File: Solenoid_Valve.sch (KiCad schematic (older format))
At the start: 60 parts, among them IC1 Si8621AB-B-ISR, J1 Conn_01x02, J10 Conn_01x05, J11 Conn_01x02, J12 Conn_01x02, J13 Conn_01x02, J14 Conn_01x02, J15 Conn_01x02, J16 Conn_01x02, J17 Conn_01x02, J18 Conn_01x02, J19 Conn_01x02, J2 Conn_01x02, J20 Bus_mechaken_PCIexpress_x16_1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, J3 Conn_01x02, J4 Conn_01x02, J5 Conn_01x03, J6 Conn_01x02, J7 Conn_01x02, J8 Conn_01x02, J9 Conn_01x02, Q1 ULN2004D1013TR, Q2 ULN2004D1013TR, Q3 ULN2004D1013TR, U1 NJM7812, U2 AP2210N-3.3TRG1, U3 STM32F042K6Tx, U4 AP2210N-3.3TRG1, U5 MCP2562-E-SN

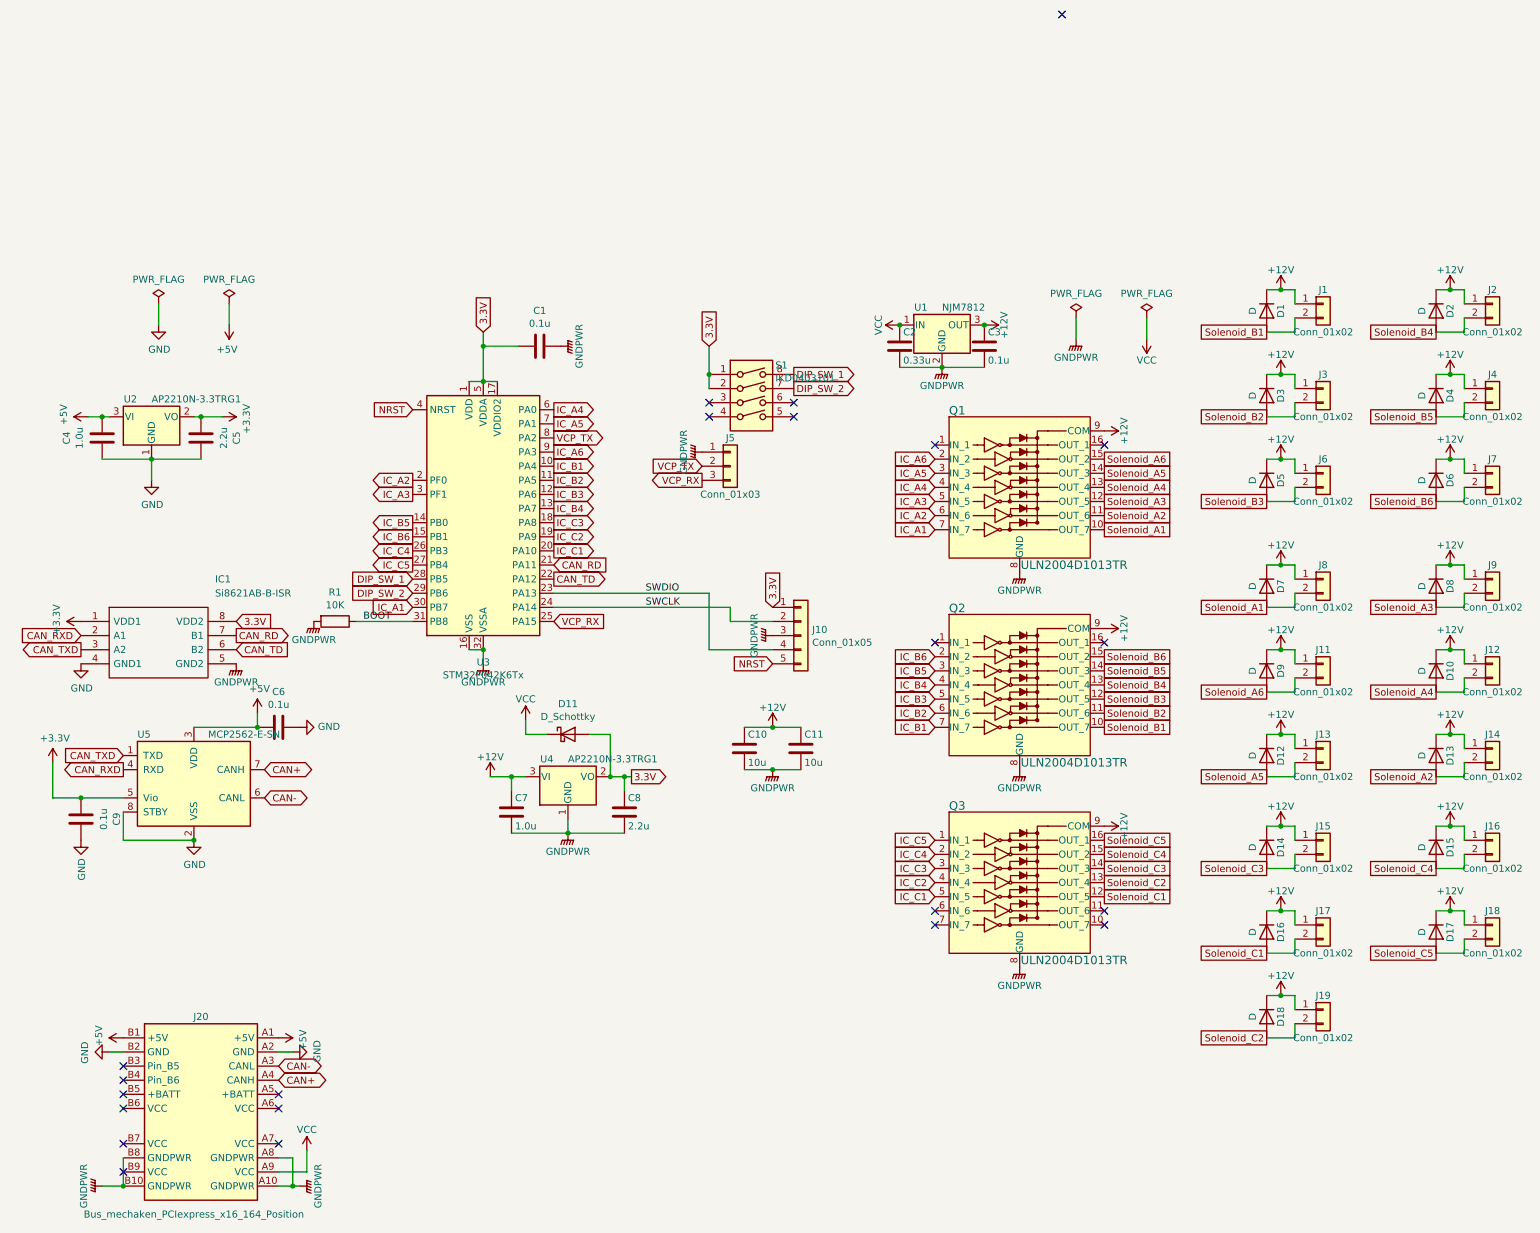
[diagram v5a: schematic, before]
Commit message: Fix: Symbol & Footprint Library
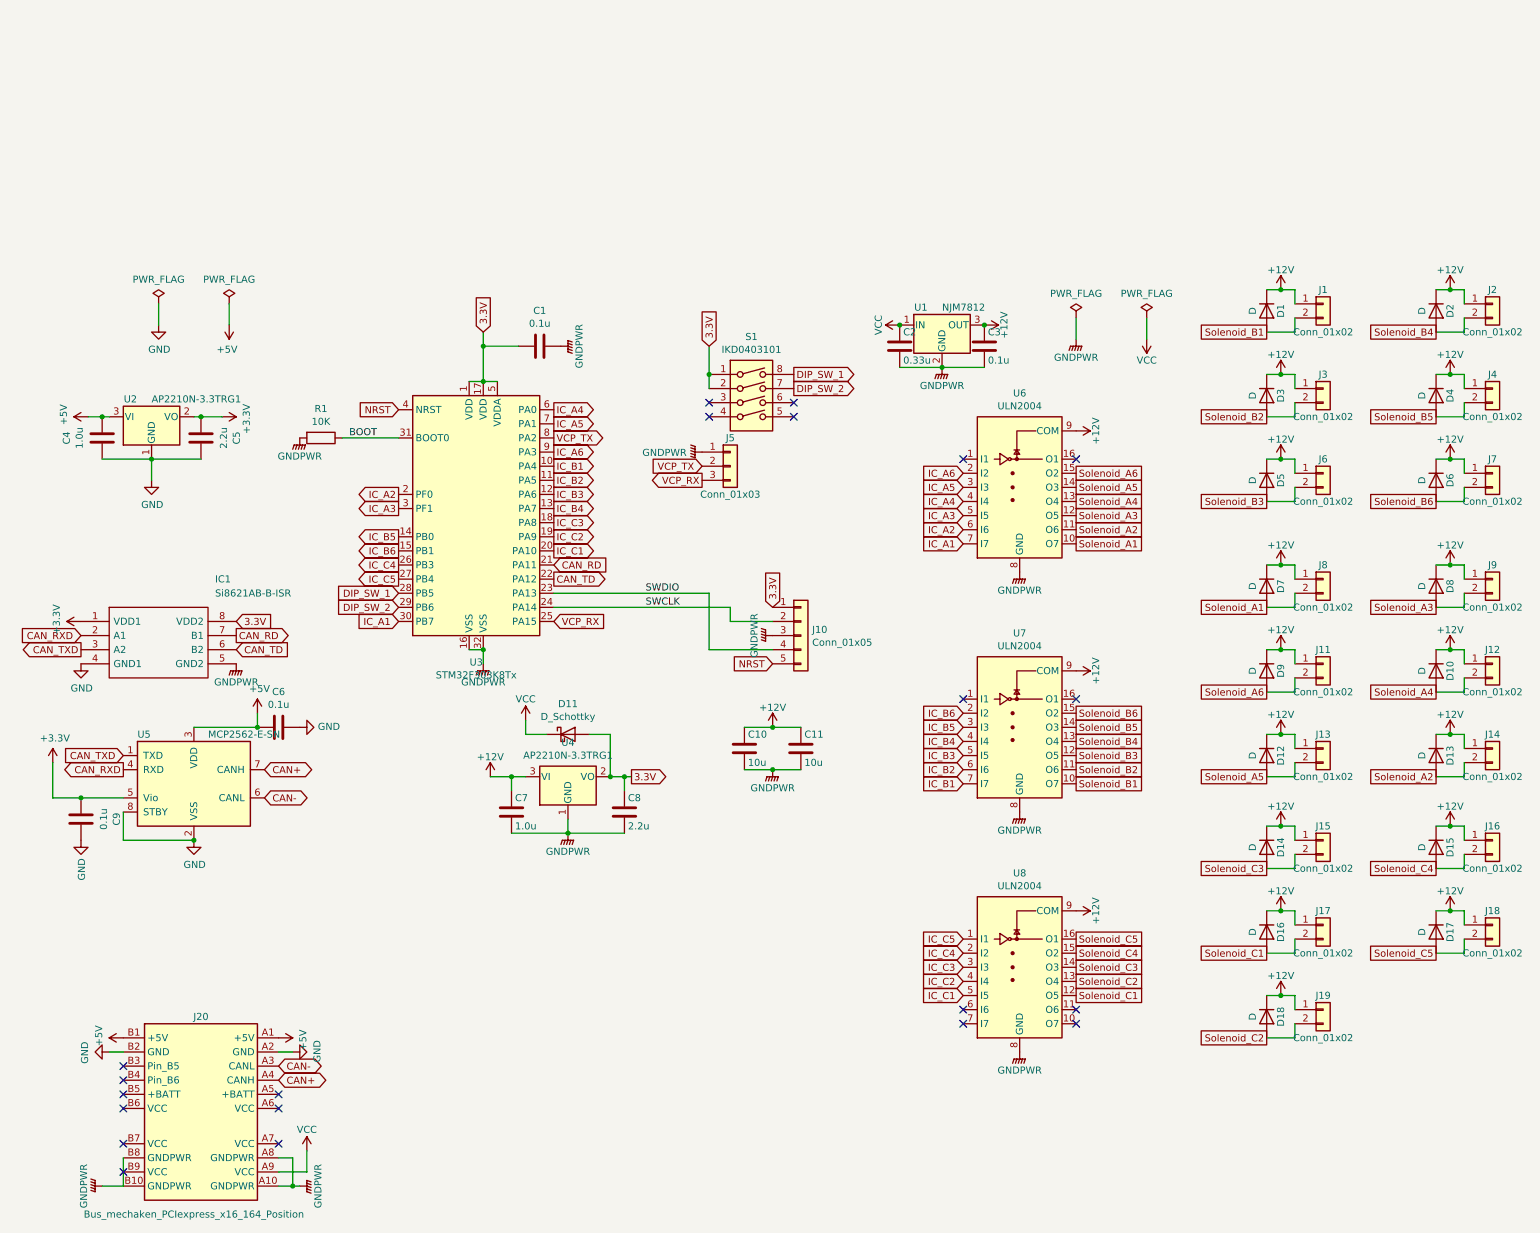
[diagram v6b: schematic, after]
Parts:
- removed Q1, Q2, Q3: ULN2004D1013TR, digikey-footprints:SOIC-16_W3.90mm, symbol Solenoid_Valve-rescue:ULN2003D1013TR-dk_Transistors-Bipolar-BJT-Arrays
- removed U3: STM32F042K6Tx, Package_QFP:LQFP-32_7x7mm_P0.8mm, symbol MCU_ST_STM32F0:STM32F042K6Tx
- added U3: STM32F303K8Tx, Package_QFP:LQFP-32_7x7mm_P0.8mm, symbol MCU_ST_STM32F3:STM32F303K8Tx
- added U6, U7, U8: ULN2004, Package_SO:SOIC-16_3.9x9.9mm_P1.27mm, symbol Transistor_Array:ULN2004
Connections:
- net +12V: now also U6.9 (COM), U7.9 (COM), U8.9 (COM)
- net 3.3V: now also U3.1 (VDD), U3.17 (VDD), U3.5 (VDDA)
- net BOOT: now also U3.31 (BOOT0)
- net CAN_RD: now also U3.21 (PA11)
- net CAN_TD: now also U3.22 (PA12)
- net DIP_SW_1: now also U3.28 (PB5)
- net DIP_SW_2: now also U3.29 (PB6)
- net GNDPWR: now also U3.16 (VSS), U3.32 (VSS), U6.8 (GND), U7.8 (GND), U8.8 (GND)
- net IC_A1: now also U3.30 (PB7), U6.7 (I7)
- net IC_A2: now also U3.2 (PF0), U6.6 (I6)
- net IC_A3: now also U3.3 (PF1), U6.5 (I5)
- net IC_A4: now also U3.6 (PA0), U6.4 (I4)
- net IC_A5: now also U3.7 (PA1), U6.3 (I3)
- net IC_A6: now also U3.9 (PA3), U6.2 (I2)
- net IC_B1: now also U3.10 (PA4), U7.7 (I7)
- net IC_B2: now also U3.11 (PA5), U7.6 (I6)
- net IC_B3: now also U3.12 (PA6), U7.5 (I5)
- net IC_B4: now also U3.13 (PA7), U7.4 (I4)
- net IC_B5: now also U3.14 (PB0), U7.3 (I3)
- net IC_B6: now also U3.15 (PB1), U7.2 (I2)
- net IC_C1: now also U3.20 (PA10), U8.5 (I5)
- net IC_C2: now also U3.19 (PA9), U8.4 (I4)
- net IC_C3: now also U3.18 (PA8), U8.3 (I3)
- net IC_C4: now also U3.26 (PB3), U8.2 (I2)
- net IC_C5: now also U3.27 (PB4), U8.1 (I1)
- net NRST: now also U3.4 (NRST)
- net SWCLK: now also U3.24 (PA14)
- net SWDIO: now also U3.23 (PA13)
- net Solenoid_A1: now also U6.10 (O7)
- net Solenoid_A2: now also U6.11 (O6)
- net Solenoid_A3: now also U6.12 (O5)
- net Solenoid_A4: now also U6.13 (O4)
- net Solenoid_A5: now also U6.14 (O3)
- net Solenoid_A6: now also U6.15 (O2)
- net Solenoid_B1: now also U7.10 (O7)
- net Solenoid_B2: now also U7.11 (O6)
- net Solenoid_B3: now also U7.12 (O5)
- net Solenoid_B4: now also U7.13 (O4)
- net Solenoid_B5: now also U7.14 (O3)
- net Solenoid_B6: now also U7.15 (O2)
- net Solenoid_C1: now also U8.12 (O5)
- net Solenoid_C2: now also U8.13 (O4)
- net Solenoid_C3: now also U8.14 (O3)
- net Solenoid_C4: now also U8.15 (O2)
- net Solenoid_C5: now also U8.16 (O1)
- net VCP_RX: now also U3.25 (PA15)
- net VCP_TX: now also U3.8 (PA2)
- no-connect marks 22 -> 21
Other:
- moved on the sheet: R1

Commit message: Update: ダーリントントランジスタアレイをULN2003に変更
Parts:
- U6, U7, U8: value ULN2004 -> ULN2003; symbol Transistor_Array:ULN2004 -> Transistor_Array:ULN2003
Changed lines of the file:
@@
 Text GLabel 3100 3000 0    50   Input ~ 0
 DIP_SW_2
-$Comp
-L Transistor_Array:ULN2004 U6
-U 1 1 5FB008BC
-P 7500 2150
-F 0 "U6" H 7500 2817 50  0000 C CNN
-F 1 "ULN2004" H 7500 2726 50  0000 C CNN
-F 2 "Package_SO:SOIC-16_3.9x9.9mm_P1.27mm" H 7550 1600 50  0001 L CNN
-F 3 "http://www.ti.com/lit/ds/symlink/uln2003a.pdf" H 7600 1950 50  0001 C CNN
-	1    7500 2150
-	1    0    0    -1
-$EndComp
 Text GLabel 7100 2550 0    50   Input ~ 0
 IC_A1
@@
 IC_A6
 $Comp
-L Transistor_Array:ULN2004 U7
+L Transistor_Array:ULN2003 U7
 U 1 1 5FB39E24
 P 7500 3850
 F 0 "U7" H 7500 4517 50  0000 C CNN
-F 1 "ULN2004" H 7500 4426 50  0000 C CNN
+F 1 "ULN2003" H 7500 4426 50  0000 C CNN
 F 2 "Package_SO:SOIC-16_3.9x9.9mm_P1.27mm" H 7550 3300 50  0001 L CNN
 F 3 "http://www.ti.com/lit/ds/symlink/uln2003a.pdf" H 7600 3650 50  0001 C CNN
@@
 $EndComp
 $Comp
-L Transistor_Array:ULN2004 U8
+L Transistor_Array:ULN2003 U8
 U 1 1 5FB343C2
 P 7500 5550
 F 0 "U8" H 7500 6217 50  0000 C CNN
-F 1 "ULN2004" H 7500 6126 50  0000 C CNN
+F 1 "ULN2003" H 7500 6126 50  0000 C CNN
 F 2 "Package_SO:SOIC-16_3.9x9.9mm_P1.27mm" H 7550 5000 50  0001 L CNN
 F 3 "http://www.ti.com/lit/ds/symlink/uln2003a.pdf" H 7600 5350 50  0001 C CNN
@@
 Text GLabel 7100 2450 0    50   Input ~ 0
 IC_A2
+$Comp
+L Transistor_Array:ULN2003 U6
+U 1 1 5FB008BC
+P 7500 2150
+F 0 "U6" H 7500 2817 50  0000 C CNN
+F 1 "ULN2003" H 7500 2726 50  0000 C CNN
+F 2 "Package_SO:SOIC-16_3.9x9.9mm_P1.27mm" H 7550 1600 50  0001 L CNN
+F 3 "http://www.ti.com/lit/ds/symlink/uln2003a.pdf" H 7600 1950 50  0001 C CNN
+	1    7500 2150
+	1    0    0    -1
+$EndComp
 $EndSCHEMATC
